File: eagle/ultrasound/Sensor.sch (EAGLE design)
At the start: 20 parts, among them IC1 LM324D, IC2 BD6211F, U1 NC7NZ04K8X

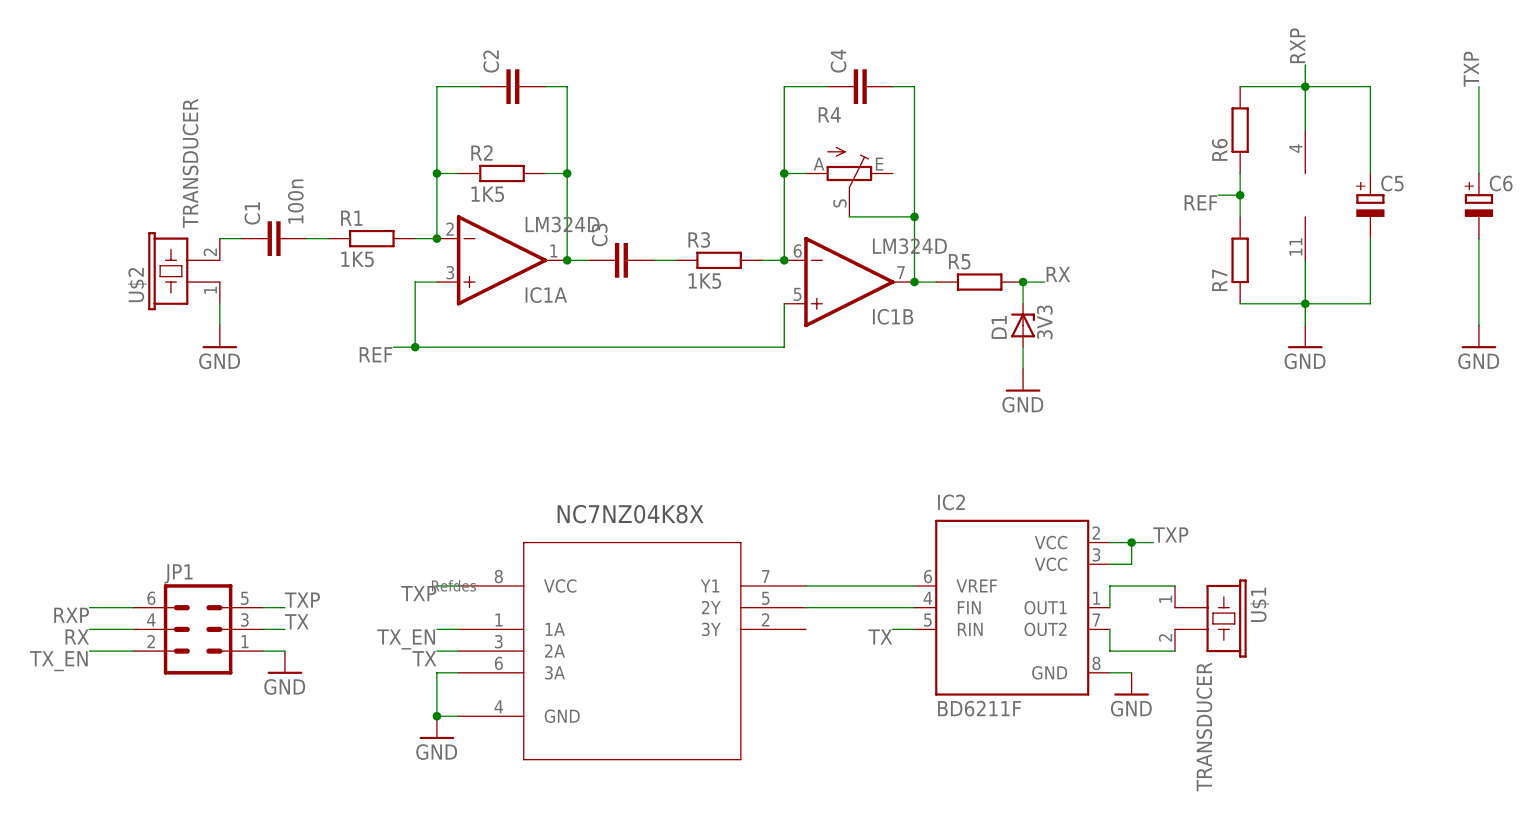
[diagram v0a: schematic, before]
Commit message: Continued design and implementation, completing all range finder diagrams.
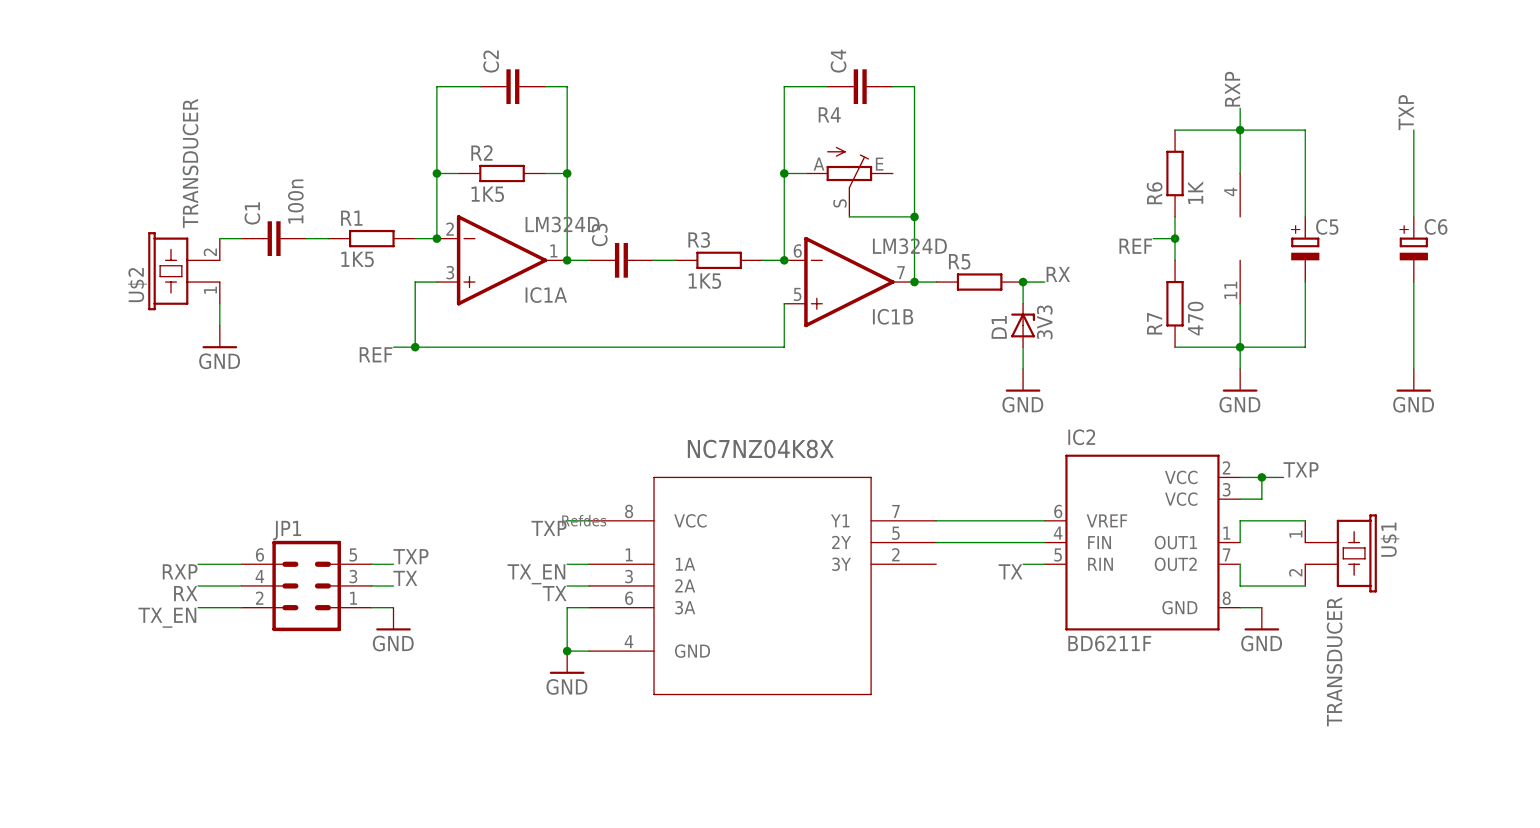
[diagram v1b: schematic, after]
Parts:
- R6: value (none) -> 1K
- R7: value (none) -> 470
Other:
- moved on the sheet: C5, C6, IC2, JP1, R6, R7, U$1

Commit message: Updated component values on daughter board schematic to match actual board.
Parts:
- C5, C6: value (none) -> 10uF
- R2: value 1K5 -> 5K6
- R4: value (none) -> 100K
- R5: value (none) -> 1K
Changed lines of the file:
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@@
 <?xml version="1.0" encoding="utf-8"?>
 <!DOCTYPE eagle SYSTEM "eagle.dtd">
-<eagle version="6.4">
+<eagle version="6.3">
 <drawing>
 <settings>
@@
 <part name="R1" library="rcl" deviceset="R-EU_" device="R0805" value="1K5"/>
 <part name="R3" library="rcl" deviceset="R-EU_" device="R0805" value="1K5"/>
-<part name="R4" library="pot" deviceset="TRIM_EU-" device="S63P"/>
+<part name="R4" library="pot" deviceset="TRIM_EU-" device="S63P" value="100K"/>
 <part name="C1" library="rcl" deviceset="C-EU" device="C0805" value="100n"/>
 <part name="C2" library="rcl" deviceset="C-EU" device="C0805"/>
 <part name="C3" library="rcl" deviceset="C-EU" device="C0805"/>
 <part name="C4" library="rcl" deviceset="C-EU" device="C0805"/>
-<part name="R5" library="rcl" deviceset="R-EU_" device="R0805"/>
+<part name="R5" library="rcl" deviceset="R-EU_" device="R0805" value="1K"/>
 <part name="GND1" library="supply1" deviceset="GND" device=""/>
 <part name="D1" library="diode" deviceset="ZENER-DIODE" device="ZD-2.5" value="3V3"/>
@@
 <part name="JP1" library="con-lstb" deviceset="MA03-2" device=""/>
 <part name="GND5" library="supply1" deviceset="GND" device=""/>
-<part name="C5" library="rcl" deviceset="CPOL-EU" device="E2-5"/>
-<part name="C6" library="rcl" deviceset="CPOL-EU" device="E2-5"/>
+<part name="C5" library="rcl" deviceset="CPOL-EU" device="E2-5" value="10uF"/>
+<part name="C6" library="rcl" deviceset="CPOL-EU" device="E2-5" value="10uF"/>
 <part name="GND6" library="supply1" deviceset="GND" device=""/>
 <part name="U$1" library="Ultrasound" deviceset="TRANSDUCER" device=""/>
@@
 <part name="R6" library="rcl" deviceset="R-EU_" device="R0805" value="1K"/>
 <part name="R7" library="rcl" deviceset="R-EU_" device="R0805" value="470"/>
-<part name="R2" library="rcl" deviceset="R-EU_" device="R0805" value="1K5"/>
+<part name="R2" library="rcl" deviceset="R-EU_" device="R0805" value="5K6"/>
 </parts>
 <sheets>

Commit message: Updated sensor board resistor value in Eagle files
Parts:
- R5: value 1K -> 100
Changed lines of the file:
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@@
 <part name="C3" library="rcl" deviceset="C-EU" device="C0805"/>
 <part name="C4" library="rcl" deviceset="C-EU" device="C0805"/>
-<part name="R5" library="rcl" deviceset="R-EU_" device="R0805" value="1K"/>
+<part name="R5" library="rcl" deviceset="R-EU_" device="R0805" value="100"/>
 <part name="GND1" library="supply1" deviceset="GND" device=""/>
 <part name="D1" library="diode" deviceset="ZENER-DIODE" device="ZD-2.5" value="3V3"/>
